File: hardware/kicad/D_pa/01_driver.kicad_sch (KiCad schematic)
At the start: 24 parts, among them J10 A kartindan TX1, Q20 IRF530N, Q21 IRF530N, T10 BN43-202 2:1, T12 BN43-202 2:3, U10 PE4312C-Z, U11 PGA-103+

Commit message: Connect the pads that had no net
A symbol pin number must agree with the footprint pad number. If the
numbers do not agree, the net goes nowhere. The netlist removes it
and gives no message. ERC examines the schematic and sees a wire. DRC
does not count an unconnected pad as a violation. All three boards
showed zero ERC violations while 31 pads had no net.

Two of these faults stopped a board.

The footprint of the Ethernet PHY was for a different part. The
project used QFN-48 6x6 mm with 0.4 mm pitch. The RTL8211F(I)-CG is
WQFN-40-EP 5x5 mm. You cannot solder the part to that pad pattern.

The 25 MHz crystal had a 2-pin symbol on a 4-pad footprint. On a 3225
crystal the terminals are the diagonal pads 1 and 3. Pads 2 and 4 are
the metal can. XO went to pad 2. There was no crystal between XI and
XO, and thus neither PHY could make a clock.

The paddle of the AD9251 was pin 0 in the symbol and pad 65 in the
footprint. The paddle of the PE4312 was Pad against pad 21. The gas
discharge tubes had one electrode unconnected, because
Device:GDT_2Pin uses pins 1 and 3 but the varistor footprint uses
pads 1 and 2. A local footprint with pads 1 and 3 corrects this.

ped_denetim.py finds these faults on the board. yap.sh runs it before
the DSN export. The chain stops if a pad has no net.

The DSN export also changed. It declared In1 and In4 as power layers
but did not export the copper on them. The router thus believed that
the two ground planes were empty. It routed the 289 pins of GND as
traces on the signal layers. The planes now go out as conduction
areas.
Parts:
- removed T12: BN43-202 2:3, dogrudan-sdr:XFMR_Toroid_4P_Vertical, symbol Device:Transformer_1P_1S
- added T12: BN43-202 2:3 CT, dogrudan-sdr:XFMR_Toroid_5P_Vertical, symbol dogrudan-sdr:XFMR_CT
- C110: footprint Capacitor_SMD:C_0603_1608Metric -> Capacitor_SMD:C_1206_3216Metric
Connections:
- net D2_CT: now also T12.5 (PRI_CT)
- net D2_DA: now also T12.1 (PRI_A)
- net D2_DB: now also T12.2 (PRI_B)
- net DRV_OUT: now also T12.3 (SEC_A)
- net GND: now also U10.21 (GND), T12.4 (SEC_B); no longer U10.Pad (GND)
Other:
- note added: "** Q20/Q21 SOGUTUCUSUZ CALISMAZ ** 12 W giris - 8 W RF = 4 W isi, cihaz basina 2 W. Sogutucusuz TO-220: Rth(j-a) 62 C/W -> 124 C artis. Kutu ici 55 C ile Tj ~180 C; IRF530N siniri 175 C. Ikisi de finallerin flansina vidalanacak: 20 C/W'lik bir kanatcikla Tj ~99 C'ye iniyor."
- note added: "SURUCU 2 AB SINIFI, A degil. Bu kat 8 W veriyor; A sinifinda 27 W isi ederdi ve hicbir sey kazandirmazdi — doğrusalligi belirleyen FINAL kat. Sabit bias, servo yok. 12 V besleme: 8 W icin 50 V gereksiz, LM5164 ile 50 V'tan uretiliyor (06_power). (Once burada '24 V' yaziyordu; 24 V rayi guc agacindan kalkti, metin bayat kalmisti.) IRF530N Ciss 920 pF — IRFP250N'in ucte biri, surulmesi kolay."
- note removed: "SURUCU 2 AB SINIFI, A degil. Bu kat 8 W veriyor; A sinifinda 27 W isi ederdi ve hicbir sey kazandirmazdi — doğrusalligi belirleyen FINAL kat. Sabit bias, servo yok. 24 V besleme: 8 W icin 50 V gereksiz, ayri bir LDO/buck ile 50 V'tan uretiliyor (06_power). IRF530N Ciss 920 pF — IRFP250N'in ucte biri, surulmesi kolay."

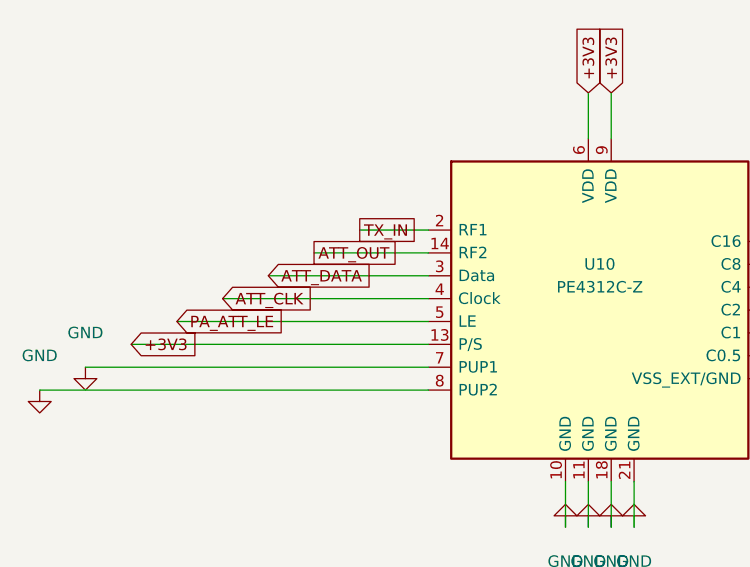
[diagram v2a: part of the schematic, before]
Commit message: Remove the pads that have no copper from the DSN export
The router reported the same 220 clearance violations in each pass.
At the same time the number of unrouted connections decreased. The
violations were thus in the input and not in the routing.

The -1EP footprints of KiCad put four paste apertures on the exposed
pad. These apertures stop full paste coverage and they have no copper
layer. The DSN export put them on the top copper layer. The image of
U51 in the DSN had 21 pins: 17 correct pins and four unconnected
copper islands in the exposed pad. These islands are always in
conflict with the pad and they close the area below it.

The export now removes a pad that has no copper layer. The image of
U51 has 17 pins. The violations on board D decreased from 220 to 152.
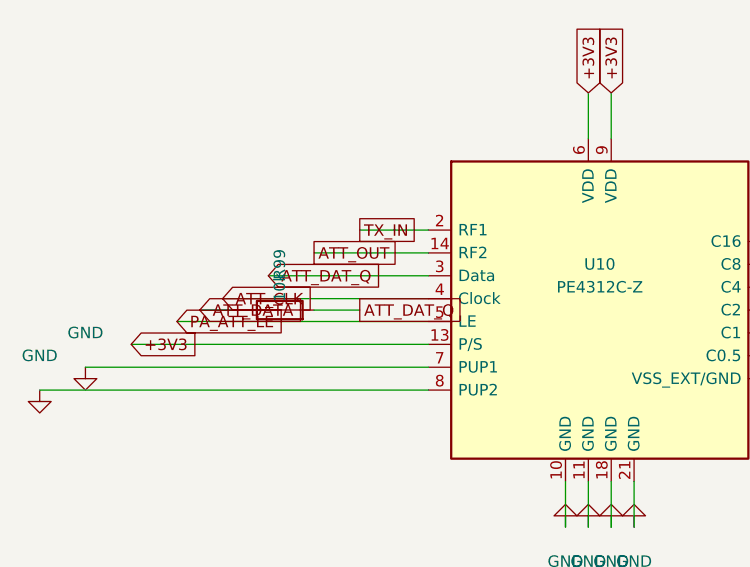
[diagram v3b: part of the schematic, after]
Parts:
- added R99: 10k, Resistor_SMD:R_0603_1608Metric, symbol Device:R
- U10: footprint Package_DFN_QFN:QFN-20-1EP_4x4mm_P0.5mm_EP2.6x2.6mm_ThermalVias -> Package_DFN_QFN:TQFN-20-1EP_4x4mm_P0.5mm_EP2.1x2.1mm_ThermalVias
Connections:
- net ATT_DATA: now also R99.1; no longer U10.3 (Data)
- new net ATT_DAT_Q: R99.2, U10.3 (Data)

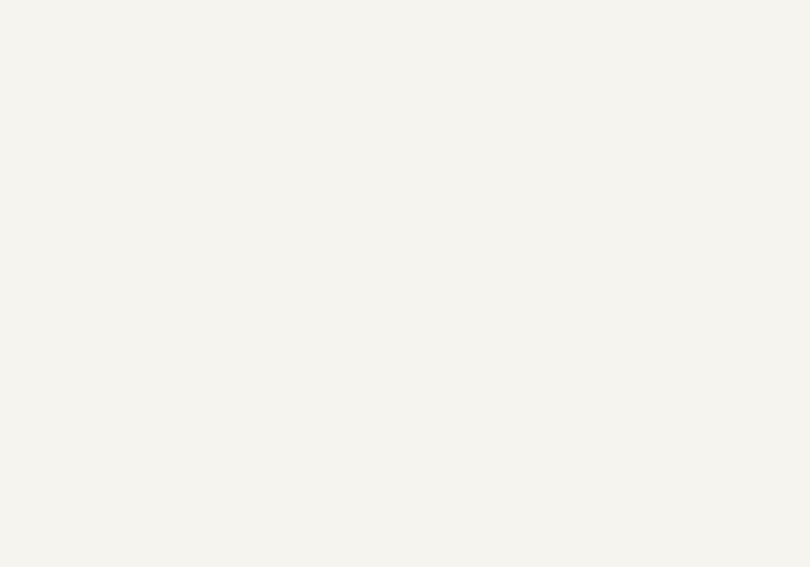
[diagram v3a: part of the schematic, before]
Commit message: Correct the clearance test for the pre-routed traces
The clearance test used a circle for each pad. The radius was
max(width, height)/2. The corner of a rectangle is at
hypot(width, height)/2 from the center. The test thus made the pad
smaller than it is. On the 2.5 x 4.5 mm gate pad of a TO-247 the
difference is 2.250 mm against 2.574 mm.

The DRN_A trace was on the gate pad of Q10 with an overlap of 35 um.
This is a short circuit between the 50 V drain rail and the gate of a
100 W device. The search that finds the tee offset accepted this
route. The overlap is at a corner and 35 um wide. You cannot see it
on a plot.

The test now uses the real shape of the pad and the collision test of
pcbnew. It also uses the 300 um clearance and not only an overlap. A
trace that is 50 um from a pad is also not possible to manufacture.

Board D was built again. No trace is below 300 um and the smallest
gap is 0.537 mm. Boards A and C were correct.
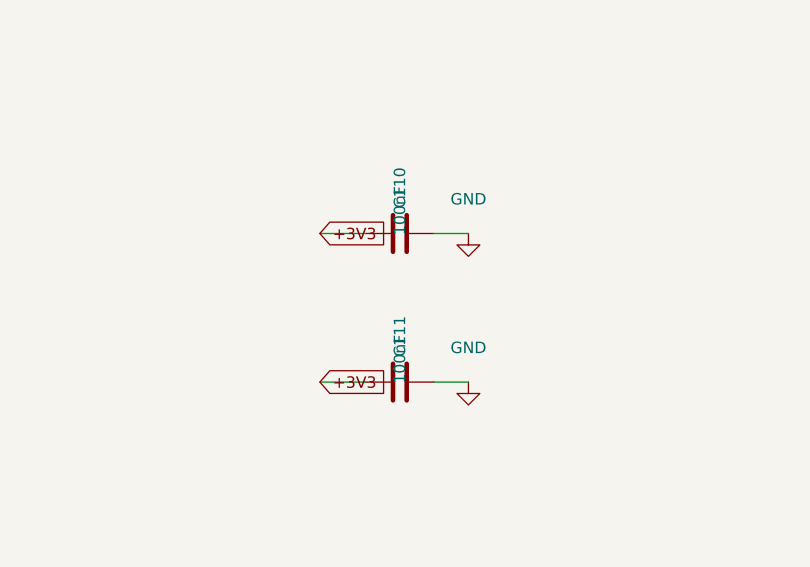
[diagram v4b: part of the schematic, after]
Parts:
- removed C110: 10uF, Capacitor_SMD:C_1206_3216Metric, symbol Device:C
- added C110: 10uF, Capacitor_SMD:C_1206_3216Metric, symbol Device:C
- added C110, C111: 100nF, Capacitor_SMD:C_0603_1608Metric, symbol Device:C
- U10: footprint Package_DFN_QFN:TQFN-20-1EP_4x4mm_P0.5mm_EP2.1x2.1mm_ThermalVias -> Package_DFN_QFN:TQFN-20-1EP_4x4mm_P0.5mm_EP2.1x2.1mm
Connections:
- net +3V3: now also C110.1, C111.1
- net D2_CT: now also C110.1
- net GND: now also C110.2, C110.2, C111.2

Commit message: Correct the schematic faults that ERC cannot find
An agent examined the three schematics against the datasheets. ERC
reported zero violations before and after this work. None of these
faults are visible to ERC.

The comparator for the external 10 MHz reference was in shutdown. The
SHDN pin of the TLV3501 went to +3V3. Sixteen DRV8833 devices had VCP
and VINT unconnected. Without the charge pump none of the 28 filter
relays can latch. Seven regulators had no decoupling capacitor within
18 mm to 94 mm. On board D the nearest +12V capacitor to an LM358 was
227 mm away on a 275 mm board.

The PE4312 devices had no series 10k resistor on pin 3. The datasheet
makes this necessary for the attenuation accuracy. Their exposed pad
was 2.6 mm against 2.15 mm. The BOM did not give the load capacitance
of the crystal. This work added 60 parts and changed 4 footprints.

The worst fault was in the tool chain. lib/gen_symbols.py still made
the old pin numbers. The five corrections went into the symbol
library by hand and not into its generator. A new library would have
removed all of them.

The thermal vias are now a decision from the measured clearance and
the dissipation. This work removed them from the PE4312, the RTL8211F
and the ADCLK846. They stay on the DRV8833 and on the LM5164, which
is a 1 W buck converter.

Two checks are new. sema_denetim compares the pin names with the
nets. netlist_denetim locks 22 pin-to-net expectations from the
datasheets and does not need a board.

The boards were built again with these corrections. The chain now
adds the test points: 10 on board A, 7 on board C and 15 on board D.
Each board has 3 fiducials. Every pad has a net.
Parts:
- removed C110: 10uF, Capacitor_SMD:C_1206_3216Metric, symbol Device:C
- removed C110: 100nF, Capacitor_SMD:C_0603_1608Metric, symbol Device:C
- added C110: 10uF, Capacitor_SMD:C_1206_3216Metric, symbol Device:C
- added C110: 100nF, Capacitor_SMD:C_0603_1608Metric, symbol Device:C
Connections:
- net +3V3: now also C110.1
- net D2_CT: now also C110.1
- net GND: now also C110.2, C110.2

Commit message: Move each decoupling capacitor to the pin it serves
The audit found 14 chips with no decoupling capacitor within 15 mm.
Across the boards the nearest capacitor to a supply rail was a median
7.5 mm on A and 6.3 mm on C, and 91 mm in the worst case. A capacitor
45 mm from its pin has about 45 nH of loop inductance, near 2.8 ohm at
10 MHz, where milliohms are necessary. It is on the schematic, it is
in the BOM, it is fitted, and it does nothing.

The pass that moves capacitors ran before the fallback placer, so a
chip with no explicit rule was not yet placed and never entered the
pool. The fallback then gave every spare capacitor to the chip with
the most pins on the rail, which is the FPGA on +3V3. Small parts got
none. The pass now runs last.

A count of missing parts was also wrong. Every pad on a rail was
counted as a supply pin, including logic inputs tied high: SRCLR on
the 74HC595, SLEEP on the DRV8833, P/S on the PE4312. Counting only
pins the netlist marks power_in, board C has 15 supply pins and 15
capacitors. Four capacitors are missing across all three boards, not
59. The AD8318 has three supply pins and had one capacitor; it now
has three. The ADCLK846 has six and had five.
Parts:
- removed C110: 10uF, Capacitor_SMD:C_1206_3216Metric, symbol Device:C
- removed C110: 100nF, Capacitor_SMD:C_0603_1608Metric, symbol Device:C
- added C110: 10uF, Capacitor_SMD:C_1206_3216Metric, symbol Device:C
- added C110: 100nF, Capacitor_SMD:C_0603_1608Metric, symbol Device:C
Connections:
- net +3V3: now also C110.1
- net D2_CT: now also C110.1
- net GND: now also C110.2, C110.2

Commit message: Do not count a bulk capacitor as decoupling
The placement pass accepted any capacitor on the rail as sufficient.
On board A the flash memory had 10 uF at 5.5 mm and 47 uF at 16.3 mm,
so the pass was satisfied. Both are bulk. The nearest 100 nF was
17.0 mm away, and at that distance the loop inductance removes the
reason to fit it.

The audit tool already used a 10 uF ceiling for this. The placer did
not, so the two disagreed, and the placer was wrong.

The pass now treats only capacitors of 1 uF and below as decoupling,
both when it asks whether a pin is served and when it selects one to
move. It also searches a ring around the pin for free space instead
of using a fixed offset.

Findings fall from 14 to 4. Board A is clean.

Also: build.sh never ran bom.py, so BOM_*.csv were hand-made files
that no step regenerated and the BOM no longer matched the schematic.
Each board's build now writes its own.
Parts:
- removed C110: 10uF, Capacitor_SMD:C_1206_3216Metric, symbol Device:C
- removed C110: 100nF, Capacitor_SMD:C_0603_1608Metric, symbol Device:C
- added C110: 100nF, Capacitor_SMD:C_0603_1608Metric, symbol Device:C
- added C110: 10uF, Capacitor_SMD:C_1206_3216Metric, symbol Device:C
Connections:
- net +3V3: now also C110.1
- net D2_CT: now also C110.1
- net GND: now also C110.2, C110.2

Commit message: Compare symbol pins against footprint pads before placement
Every fault that would have stopped a board in this work sits in one
layer: a symbol pin number that does not agree with a footprint pad
number. The ADC paddle was pin 0 against pad 65. The attenuator
paddle was named Pad against pad 21. The gas discharge tubes used
pins 1 and 3 against pads 1 and 2. The crystal had two pins on a
four-pad part, so XO went to the can. The Ethernet PHY carried the
footprint of a different package. Each was found separately, by hand,
after it had already cost placement and routing time.

temel_denetim checks the whole class at once. For each part it
reports pins with no pad, where the net goes nowhere while the
schematic looks correct; pads with no pin, where copper is left
unconnected; and a count mismatch, which is the quickest sign that a
footprint belongs to another part.

It reads the symbols embedded in the schematics and not the library
file, because the library was edited by hand while its generator
stayed behind.

yap.sh runs it after pcb_kur and before placement, and stops there. A
wrong schematic makes everything below it worthless.

All three boards report zero. The parts it cannot check are those
with no symbol: mounting holes, fiducials and test points.
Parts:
- removed C110: 100nF, Capacitor_SMD:C_0603_1608Metric, symbol Device:C
- removed C110: 10uF, Capacitor_SMD:C_1206_3216Metric, symbol Device:C
- added C110: 10uF, Capacitor_SMD:C_1206_3216Metric, symbol Device:C
- added C110: 100nF, Capacitor_SMD:C_0603_1608Metric, symbol Device:C
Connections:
- net +3V3: now also C110.1
- net D2_CT: now also C110.1
- net GND: now also C110.2, C110.2; no longer U11.4 (GND_TAB)
